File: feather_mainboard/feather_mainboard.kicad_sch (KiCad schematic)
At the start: 4 parts

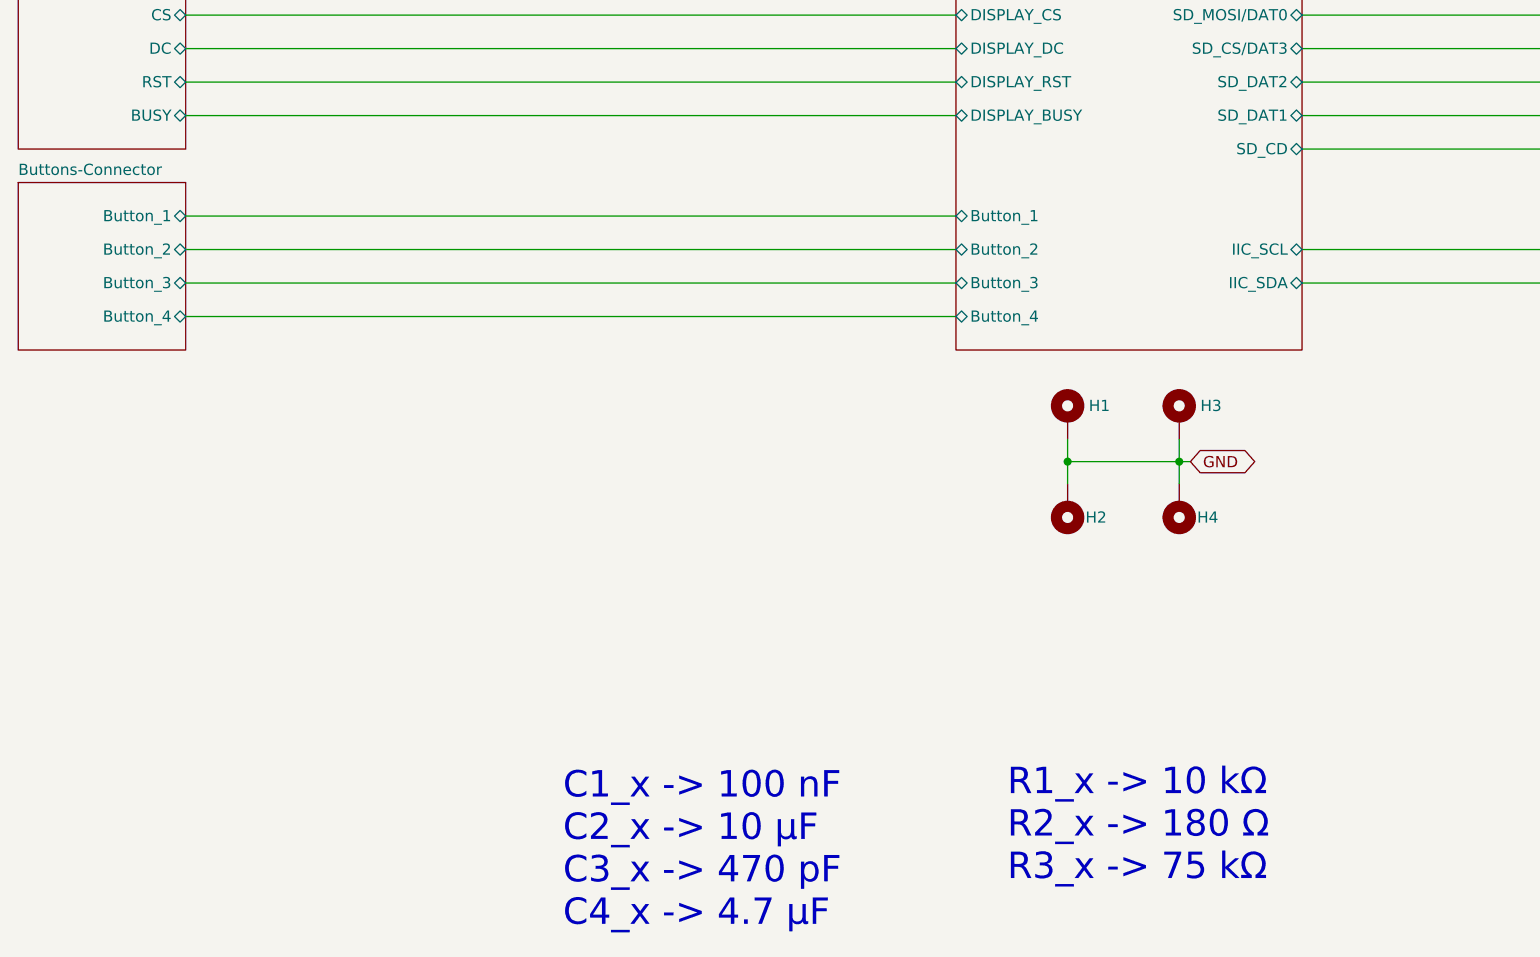
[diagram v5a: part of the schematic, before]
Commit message: changed the connector on the daughter board
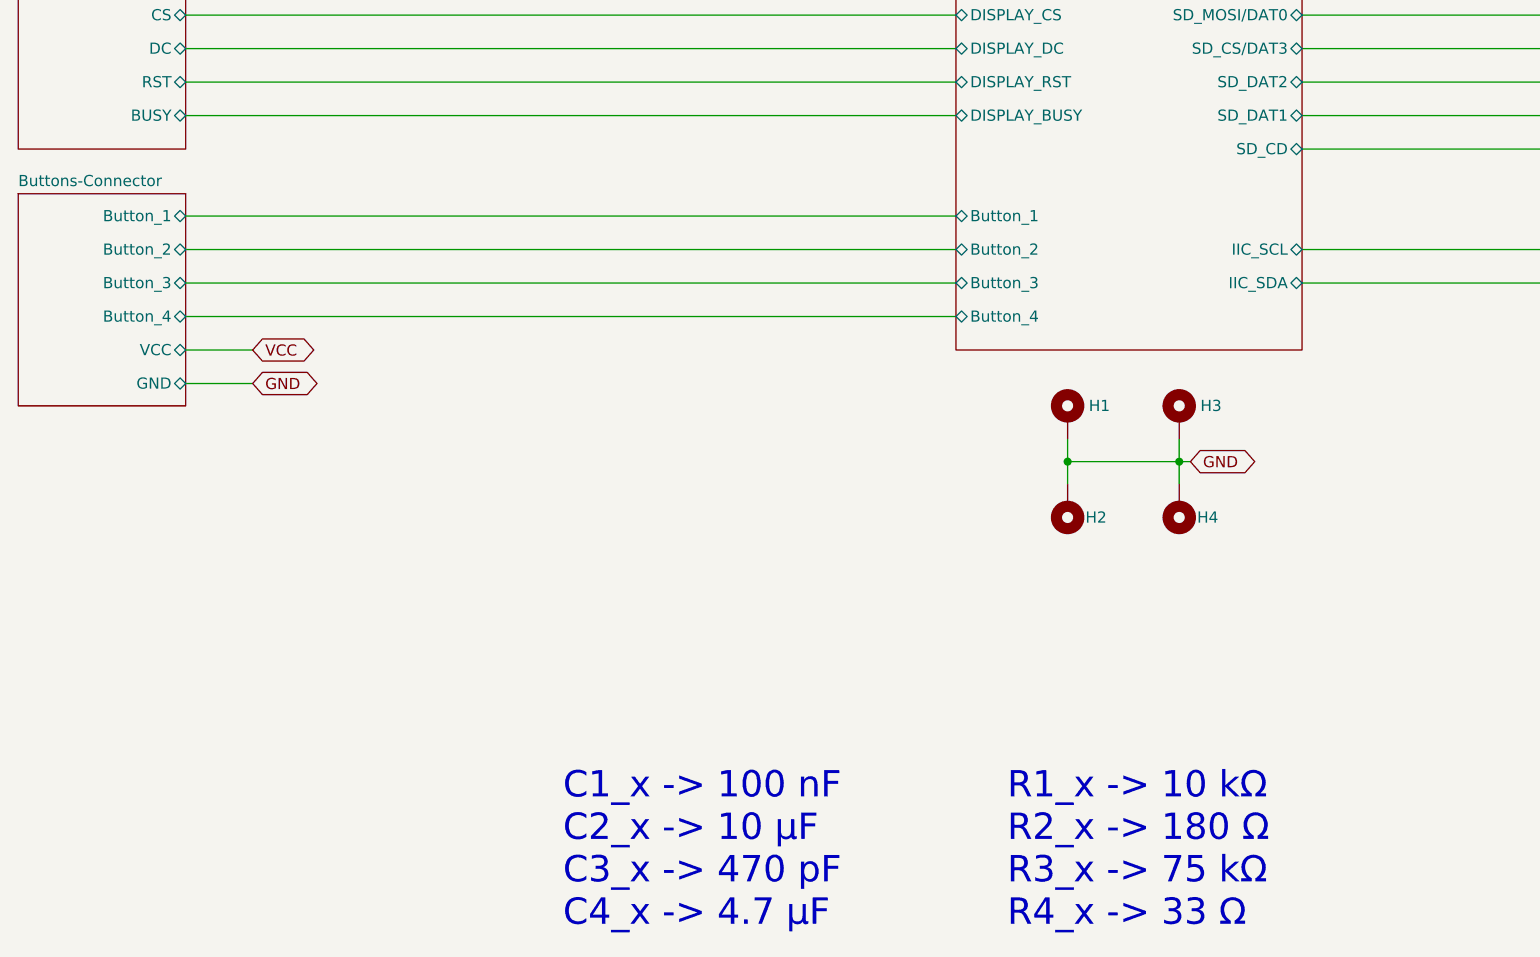
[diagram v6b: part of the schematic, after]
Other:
- sheet Buttons-Connector ports: added GND, VCC; removed none
- note added: "R1_x -> 10 kΩ R2_x -> 180 Ω R3_x -> 75 kΩ R4_x -> 33 Ω"
- note removed: "R1_x -> 10 kΩ R2_x -> 180 Ω R3_x -> 75 kΩ"
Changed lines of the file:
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@@
+	(wire
+		(pts
+			(xy 53.34 130.81) (xy 45.72 130.81)
+		)
+		(stroke
+			(width 0)
+			(type default)
+		)
+	)
 	(wire
 		(pts
@@
 		(pts
 			(xy 125.73 63.5) (xy 133.35 63.5)
+		)
+		(stroke
+			(width 0)
+			(type default)
+		)
+	)
+	(wire
+		(pts
+			(xy 53.34 134.62) (xy 45.72 134.62)
 		)
 		(stroke
@@
 		)
 	)
-	(text "R1_x -> 10 kΩ\nR2_x -> 180 Ω \nR3_x -> 75 kΩ"
+	(text "R1_x -> 10 kΩ\nR2_x -> 180 Ω \nR3_x -> 75 kΩ\nR4_x -> 33 Ω"
 		(exclude_from_sim no)
-		(at 139.192 184.912 0)
+		(at 139.192 187.706 0)
 		(effects
 			(font
@@
 	(global_label "GND"
 		(shape bidirectional)
-		(at 125.73 63.5 180)
+		(at 53.34 134.62 0)
 		(fields_autoplaced yes)
 		(effects
@@
 				(size 1.27 1.27)
 			)
+			(justify left)
+		)
+		(property "Intersheetrefs" "${INTERSHEET_REFS}"
+			(at 61.307 134.62 0)
+			(effects
+				(font
+					(size 1.27 1.27)
+				)
+				(justify left)
+				(hide yes)
+			)
+		)
+	)
+	(global_label "GND"
+		(shape bidirectional)
+		(at 125.73 63.5 180)
+		(fields_autoplaced yes)
+		(effects
+			(font
+				(size 1.27 1.27)
+			)
 			(justify right)
 		)
@@
 				)
 				(justify right)
+				(hide yes)
+			)
+		)
+	)
+	(global_label "VCC"
+		(shape bidirectional)
+		(at 53.34 130.81 0)
+		(fields_autoplaced yes)
+		(effects
+			(font
+				(size 1.27 1.27)
+			)
+			(justify left)
+		)
+		(property "Intersheetrefs" "${INTERSHEET_REFS}"
+			(at 61.0651 130.81 0)
+			(effects
+				(font
+					(size 1.27 1.27)
+				)
+				(justify left)
 				(hide yes)
 			)
@@
 	)
 	(sheet
-		(at 26.67 111.76)
-		(size 19.05 19.05)
+		(at 26.67 113.03)
+		(size 19.05 24.13)
 		(fields_autoplaced yes)
 		(stroke
@@
 		)
 		(property "Sheetname" "Buttons-Connector"
-			(at 26.67 111.0484 0)
+			(at 26.67 112.3184 0)
 			(effects
 				(font
@@
 		)
 		(property "Sheetfile" "buttons-connector.kicad_sch"
-			(at 26.67 131.3946 0)
+			(at 26.67 137.7446 0)
 			(effects
 				(font
@@
 			(effects
 				(font
+					(size 1.27 1.27)
+				)
+				(justify right)
+			)
+		)
+		(pin "VCC" bidirectional
+			(at 45.72 130.81 0)
+			(effects
+				(font
+					(size 1.27 1.27)
+				)
+				(justify right)
+			)
+		)
+		(pin "GND" bidirectional
+			(at 45.72 134.62 0)
+			(effects
+				(font

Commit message: finished mainboard and daughterboard
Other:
- company: (none) -> bklaric
- title: (none) -> Feather Mainboard
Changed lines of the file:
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@@
 	(generator_version "8.0")
 	(paper "A4")
+	(title_block
+		(title "Feather Mainboard")
+		(date "2024-10-30")
+		(rev "1")
+		(company "bklaric")
+		(comment 4 "lprd_feather_mainboard")
+	)
 	(junction
 		(at 102.87 74.93)

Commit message: added bigger logo and labeled the pins on the connectors
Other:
- company: bklaric -> Benjamin Klaric
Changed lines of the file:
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@@
 		(date "2024-10-30")
 		(rev "1")
-		(company "bklaric")
+		(company "Benjamin Klaric")
 		(comment 4 "lprd_feather_mainboard")
 	)
